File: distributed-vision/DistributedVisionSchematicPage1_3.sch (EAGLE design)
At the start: 131 parts, among them J1 RASPBERRRY_COMPUTE_CM3, J2 RASPBERRRY_COMPUTE_CM3, J3 XS10, J6 DM3D-SF, J7 10029449-111RLF, J8 1-84952-5, J9 1-84952-5, Q1 AP2331SA-7, Q2 BSS127, Q3 BSS127, Q4 BSS127, Q5 PSMN014-40YS, U1 TPS70625DBVR, U2 LM26420XMH, U4 ESD224, X1 JST-XH-02-PIN-LONG-PAD

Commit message: Combined all Schematic Pages
Fixed some Capacitor/Resistor Values
Began integrating POE
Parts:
- added C14, C64: 1u, rcl:C-USC0402
- added C53, C54, C59, C60, C63, C68: 100n, rcl:C-USC0402
- added C55, C61, C67: 10n, rcl:C-USC0402
- added C56: 1nF, rcl:C-USC0402
- added C57, C73: 10u, rcl:C-USC0402
- added C62: 4u7, rcl:C-USC0402
- added C65, C66: 33p, rcl:C-USC0402
- added C74: 22n, rcl:C-USC0402
- added IC1: IPB180N06S4-H1, infineon:IPB180N06S4-H1
- added J10: USBR-A-D-F-O-TH, distributed-vision:USBR-A-D-F-O-TH
- added J11: (no value), con-amp:215875-3
- added J12: ARJM11C7-104-AB-EW2, ethernet_poe_v2.1:ARJM11C7-104-AB-EW2
- added J4: RASPBERRRY_COMPUTE_CM3, distributed-vision:RASPBERRRY_COMPUTE_CM3
- added J5: 1981584-1, RoboJackets-Connectors:1981584-1
- added L3, L6: 2A 120r, RoboJackets-Inductors:INDUCTOR_0805
- added L4, L7: 1.3A 120r, RoboJackets-Inductors:INDUCTOR_0805
- added LED1, LED2, LED3: LAP4-BOTTOM, led:LAP4-BOTTOM
- added Q6: 25 MHz, crystal:FA-20H
- added R18: 47k, RoboJackets-Resistors:ERJ-L06KF50MV
- added R19, R28, R31, R40, R51: 4k7, RoboJackets-Resistors:ERJ-L06KF50MV
- added R26: 12k, RoboJackets-Resistors:ERJ-L06KF50MV
- added R27: 12k4, RoboJackets-Resistors:ERJ-L06KF50MV
- added R29, R30, R32: 470r, RoboJackets-Resistors:ERJ-L06KF50MV
- added R33, R34, R35, R36: 49r9, RoboJackets-Resistors:ERJ-L06KF50MV
- added R37: 10r, RoboJackets-Resistors:ERJ-L06KF50MV
- added R39, R41: 1M, RoboJackets-Resistors:ERJ-L06KF50MV
- added T1, T2: (no value), transistor:MUN2211T1-NPN_DRIVER-SC59-BEC
- added U3: LAN9513-JZXQFN64_9X9MC_MCH-M, distributed-vision:LAN9513-JZXQFN64_9X9MC_MCH-M
- added U5: FSUSB42MUX, distributed-vision:FSUSB42MUX
- added U6, U7, U8, U9: SP3003-02, distributed-vision:SP3003-02
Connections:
- new net N$55: C64.1, L4.1, U3.VDD18USBPLL
- new net N$56: C63.1, L4.2, U3.VDD18ETHPLL
- new net N$57: R29.PIN2, U3.NFDX_LED/GPIO0
- new net N$58: R30.PIN2, U3.NLNKA_LED/GPIO1
- new net N$59: R32.PIN2, U3.NSPD_LED/GPIO2
- new net N$60: LED3.C, R29.PIN1
- new net N$61: C53.1, R31.PIN1, T1.C, T2.C, U3.NRESET
- new net N$62: T1.B, T2.B
- new net N$63: R40.PIN1, U3.NTRST, U3.TCK, U3.TDI, U3.TMS
- new net N$64: Q6.2, U3.XI
- new net N$65: Q6.4, U3.XO
- new net N$66: C66.1, Q6.1, R39.PIN2
- new net N$67: C65.1, Q6.3, R39.PIN1
- new net N$68: IC1.D, R18.PIN1, U5.SEL
- new net N$69: R26.PIN1, U3.USBRBIAS
- new net N$70: R28.PIN1, U3.AUTOMDIX_EN
- new net N$71: R27.PIN1, U3.EXRES
- new net N$72: J5.1, L3.2, U6.VCC
- new net N$73: C57.1, C59.1, C67.1, J11.1, L6.2, U7.VCC
- new net N$74: C74.1, J12.CT, R37.PIN1
- new net N$75: C54.1, C55.1, R18.PIN2
- new net VCC: IC1.G, J12.G_LED+, J12.Y_LED+, L3.1, L6.1, L7.1, LED1.A, LED2.A, LED3.A, R19.PIN1, R28.PIN2, R31.PIN2, R33.PIN2, R34.PIN2, R35.PIN2, R36.PIN2, R37.PIN2, R40.PIN2, U3.TEST3, U3.VBUS_DET, U3.VDD33A, U3.VDD33IO, U5.VCC
- net FB1: now also J2D.NC@1, J2D.NC@2; no longer J2D.SDX_VDD, J2D.SDX_VDD1
- net GND: now also C14.2, C53.2, C54.2, C55.2, C56.1, C56.2, C57.2, C59.2, C60.2, C61.2, C62.2, C63.2, C64.2, C65.2, C66.2, C67.2, C68.2, C73.2, C74.2, IC1.S, J10.BGND, J10.TGND, J11.4, J12.CHASSIS1, J12.CHASSIS2, J5.5, J5.SHIELD, R19.PIN2, R26.PIN2, R27.PIN2, R41.PIN1, R41.PIN2, R51.PIN2, T1.E, T2.E, U3.CLK24_EN, U3.TEST2, U5.!OE, U5.GND, U7.GND, U8.GND, U9.GND
- net N$1: now also C14.1, C60.1, C61.1, C62.1, U3.VDD18CORE
- net N$17: now also J4A.USB_DP, U5.D+
- net N$18: now also J4A.USB_DM, U5.D-
- net N$19: now also J4A.USB_OTGID, R51.PIN1
- net N$22: now also U3.USBDP0, U5.HSD2+
- net N$23: now also U3.USBDM0, U5.HSD2-
- net N$26: now also J5.3, U5.HSD1+, U6.IO1
- net N$27: now also J5.2, U5.HSD1-, U6.IO2
- net N$29: now also J10.BD-, U3.USBDM2, U9.IO1
- net N$30: now also J10.BD+, U3.USBDP2, U9.IO2
- net N$31: now also J10.TD-, U3.USBDM3, U8.IO1, U8.IO2
- net N$32: now also J10.TD+, U3.USBDP3
- net N$34: now also J12.TD+, R33.PIN1, U3.TXP
- net N$35: now also J12.TD-, R34.PIN1, U3.TXN
- net N$36: now also J11.2, U3.USBDM4, U7.IO1, U7.IO2
- net N$37: now also J11.3, U3.USBDP4
- net N$38: now also J12.RD+, R35.PIN1, U3.RXP
- net N$39: now also J12.RD-, R36.PIN1, U3.RXN
- net N$41: now also J10.BVCC
- net N$42: now also C68.1, C73.1, J10.TVCC, L7.2, U8.VCC, U9.VCC
- net N$8: now also J12.G_LED-, LED2.C, R30.PIN1
- net N$9: now also J12.Y_LED-, LED1.C, R32.PIN1
- net SD_CLK: now also J2D.NC@3; no longer J2D.SDX_CLK
- net SD_CMD: now also J2D.NC@4; no longer J2D.SDX_CMD
- net SD_DAT0: now also J2D.NC@5; no longer J2D.SDX_D0
- net SD_DAT1: now also J2D.NC@6; no longer J2D.SDX_D1
- net SD_DAT2: now also J2D.NC@7; no longer J2D.SDX_D2
- net SD_DAT3: now also J2D.NC@8; no longer J2D.SDX_D3

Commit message: Cleaning up Schematic
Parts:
- removed C1, C2, C30, C31, C32: (no value), rcl:C-USC0603
- removed DQ1, DQ2, DQ6: GREEN, RoboJackets-LEDs:LED-GREEN0603
- removed J4: RASPBERRRY_COMPUTE_CM3, distributed-vision:RASPBERRRY_COMPUTE_CM3
- removed R15, R17, R2, R3, R45, R5, R6: (no value), rcl:R-US_R0603
- removed T2: (no value), transistor:MUN2211T1-NPN_DRIVER-SC59-BEC
- removed U1: TPS70625DBVR, distributed-vision:TPS70625DBVR
- removed VD4: 60V, RoboJackets-Diodes:DFLS160-7
- added C75, C86: (no value), rcl:C-USC0603
- added D1, D2, D6: GREEN, RoboJackets-LEDs:LED-GREEN0603
- added D4: 60V, RoboJackets-Diodes:DFLS160-7
- added R38, R42, R43, R46, R47, R48: (no value), rcl:R-US_R0603
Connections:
- net N$10 renamed GPIO17
- net N$11 renamed GPIO26
- net N$12 renamed CAM1_CP
- net N$13 renamed CAM1_CN
- net N$14 renamed CAM1_DP1
- net N$15 renamed CAM1_DN1
- net N$16 renamed CAM1_DP0
- net N$20 renamed CAM0_DN1
- net N$21 renamed CAM0_DP1
- net N$24 renamed HDMI_D2_P
- net N$25 renamed HDMI_D2_N
- net N$28 renamed HDMI_D0_P
- net N$3 renamed GPIO11
- net N$43 renamed HDMI_CLK_N
- net N$44 renamed 5V/R53
- net N$6 renamed GPIO10
- net N$7 renamed GPIO09
- removed net N$2: C1.1, J1B.GPIO0-27_VDD@1, J1B.GPIO0-27_VDD@2, R2.2, R3.2
- removed net N$29: J10.BD-, J2A.HDMI_D0_N, J7.9, U3.USBDM2, U9.IO1
- removed net N$4: C2.1, J1B.GPIO28-45_VDD@1, J1B.GPIO28-45_VDD@2, R5.2, R6.2
- removed net N$54: J2A.HDMI_SCL, J7.15, R54.1, U4.IO3_C
- removed net N$62: T1.B, T2.B
- new net 3V3: C3.1, J3.3V3@1, J3.3V3@2
- new net 5V/R54: J7.15
- new net CAM0_CN: J2A.CAM0_CN, J9.8
- new net CAM0_CP: J2A.CAM0_CP, J9.9
- new net CAM0_DN0: J2A.CAM0_DN0, J9.2
- new net CAM0_DP0: J2A.CAM0_DP0, J9.3
- new net CAM1_DN0: J2A.CAM1_DN0, J8.2
- new net GPIO22: J2A.GPIO22
- new net GPIO27: J2A.GPIO27, J3.GPIO27
- new net HDMI_CLK_P: J2A.HDMI_CLK_P, J7.10
- new net HDMI_D0_N: J2A.HDMI_D0_N, J7.9
- new net HDMI_D1_N: J2A.HDMI_D1_N, J7.6
- new net HDMI_D1_P: J2A.HDMI_D1_P, J7.4
- new net HDMI_SCL: J2A.HDMI_SCL, R54.1, U4.IO3_C
- new net N$12: C75.1, J2B.GPIO0-27_VDD@1, J2B.GPIO0-27_VDD@2, R38.2, R42.2
- new net N$17/1.6C: J2A.USB_DP
- new net N$18/1.6B: J2A.USB_DM
- new net N$24: C86.1, J2B.GPIO28-45_VDD@1, J2B.GPIO28-45_VDD@2, R43.2, R46.2
- new net NS$19/1.6B: J2A.USB_OTGID
- new net USBDM2: J10.BD-, U3.USBDM2, U9.IO1
- new net USBDP2: U3.USBDP2
- net +1.8V: now also J2B.1V8@1, J2B.1V8@2, J2B.1V8@3, J2B.1V8@4, R38.1, R43.1; no longer J1B.1V8@1, J1B.1V8@2, J1B.1V8@3, J1B.1V8@4, R3.1, R6.1
- net +2.5V: no longer C31.1, C32.1, R45.2, U1.OUT
- net +5V: now also D2.A, D4.A, D4.C, R47.1; no longer DQ2.A, R15.1, VD4.A, VD4.C
- net EMMC_DISABLE_N: now also J2A.!EMMC_DISABLE; no longer J1A.!EMMC_DISABLE
- net EMMC_EN_N_1V8: now also J2B.EMMC_EN_N_1V8; no longer J1B.EMMC_EN_N_1V8
- net FB1: now also D1.A, D6.A, J2B.3V3@1, J2B.3V3@2, J2B.3V3@3, J2B.3V3@4, J2D.SDX_VDD, J2D.SDX_VDD1, R42.1, R46.1, R48.1; no longer C3.1, C30.1, DQ1.A, DQ6.A, J1B.3V3@1, J1B.3V3@2, J1B.3V3@3, J1B.3V3@4, J2D.NC@1, J2D.NC@2, J3.3V3@1, J3.3V3@2, R17.1, R2.1, R45.1, R5.1, U1.EN, U1.IN
- net GND: now also C75.2, C86.2, J3.GND@7, U6.GND; no longer C1.2, C2.2, C30.2, C31.2, C32.2, T2.E, U1.GND
- net N$17: no longer J2A.CAM1_DN0, J4A.USB_DP, J8.2
- net N$18: no longer J2A.CAM0_DN0, J4A.USB_DM, J9.2
- net N$19: no longer J2A.CAM0_DP0, J4A.USB_OTGID, J9.3
- net N$22: no longer J2A.CAM0_CN, J9.8
- net N$23: no longer J2A.CAM0_CP, J9.9
- net N$26: no longer J2A.HDMI_D1_P, J7.4
- net N$27: no longer J2A.HDMI_D1_N, J7.6
- net N$30: no longer U3.USBDP2
- net N$32: now also D6.C; no longer DQ6.C
- net N$34: now also D1.C; no longer DQ1.C
- net N$35: now also D2.C; no longer DQ2.C
- net N$42: no longer J2A.HDMI_CLK_P, J7.10
- net N$61: no longer T2.C
- net N$8: no longer J2A.GPIO22, J3.GPIO22
- net N$9: no longer J2A.GPIO27, J3.GPIO27
- net SD_CLK: now also J2D.SDX_CLK; no longer J2D.NC@3
- net SD_CMD: now also J2D.SDX_CMD; no longer J2D.NC@4
- net SD_DAT0: now also J2D.SDX_D0; no longer J2D.NC@5
- net SD_DAT1: now also J2D.SDX_D1; no longer J2D.NC@6
- net SD_DAT2: now also J2D.SDX_D2; no longer J2D.NC@7
- net SD_DAT3: now also J2D.SDX_D3; no longer J2D.NC@8
- net VBATT: now also J2B.VBAT@1, J2B.VBAT@2, J2B.VBAT@3, J2B.VBAT@4, R47.2, R48.2; no longer J1B.VBAT@1, J1B.VBAT@2, J1B.VBAT@3, J1B.VBAT@4, R15.2, R17.2
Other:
- note removed: "DAC VCC"
- moved on the sheet: C10, C102, C103, C12, C13, C15, C16, C17, C18, C19, C20, C21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

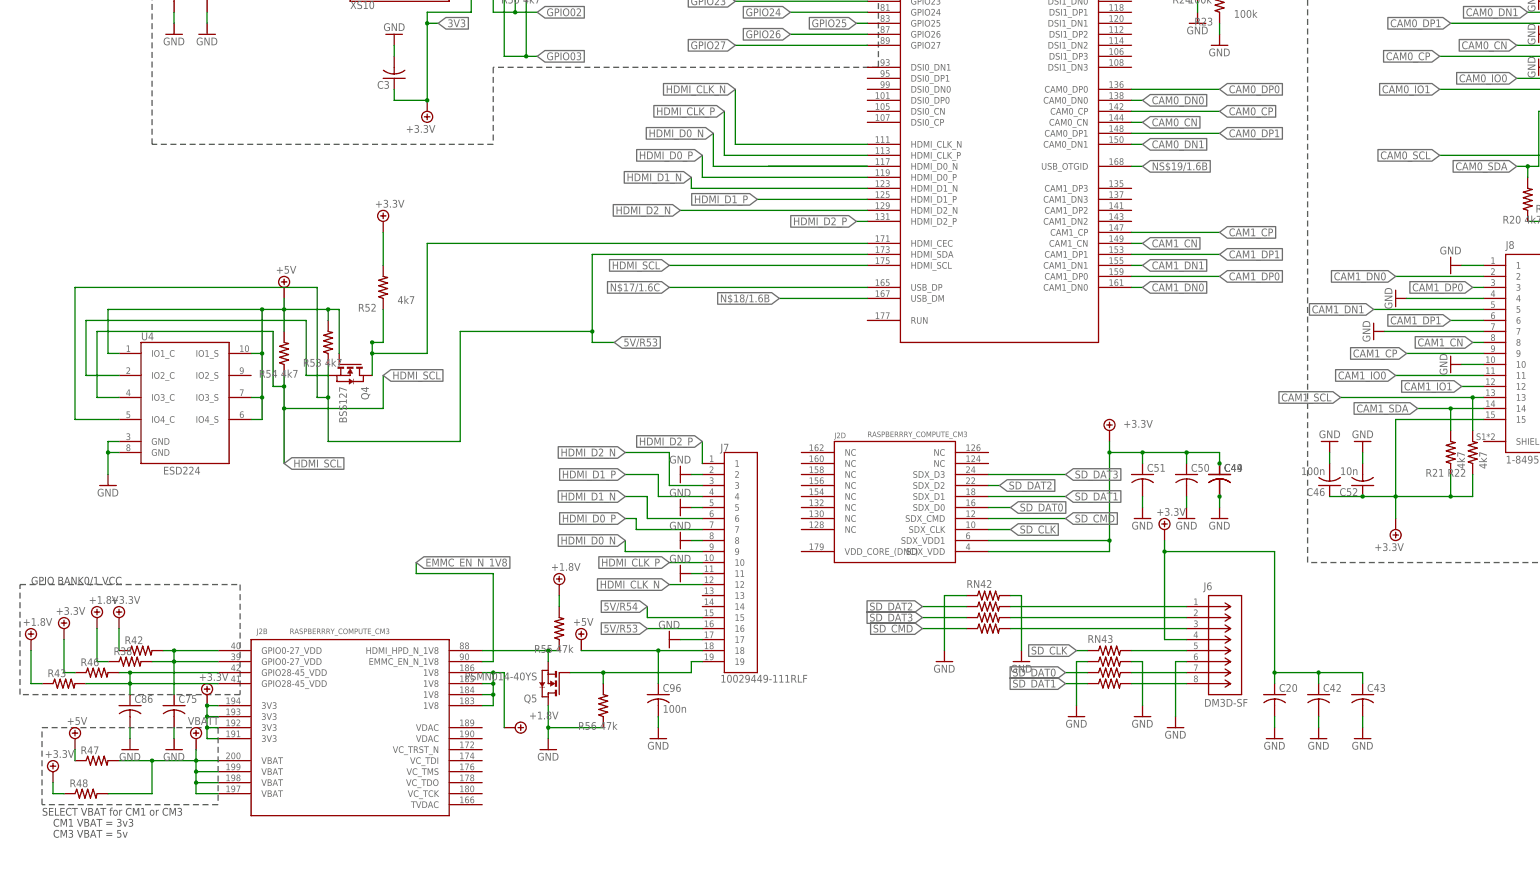
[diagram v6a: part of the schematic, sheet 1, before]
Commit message: Cleaned up Schematic
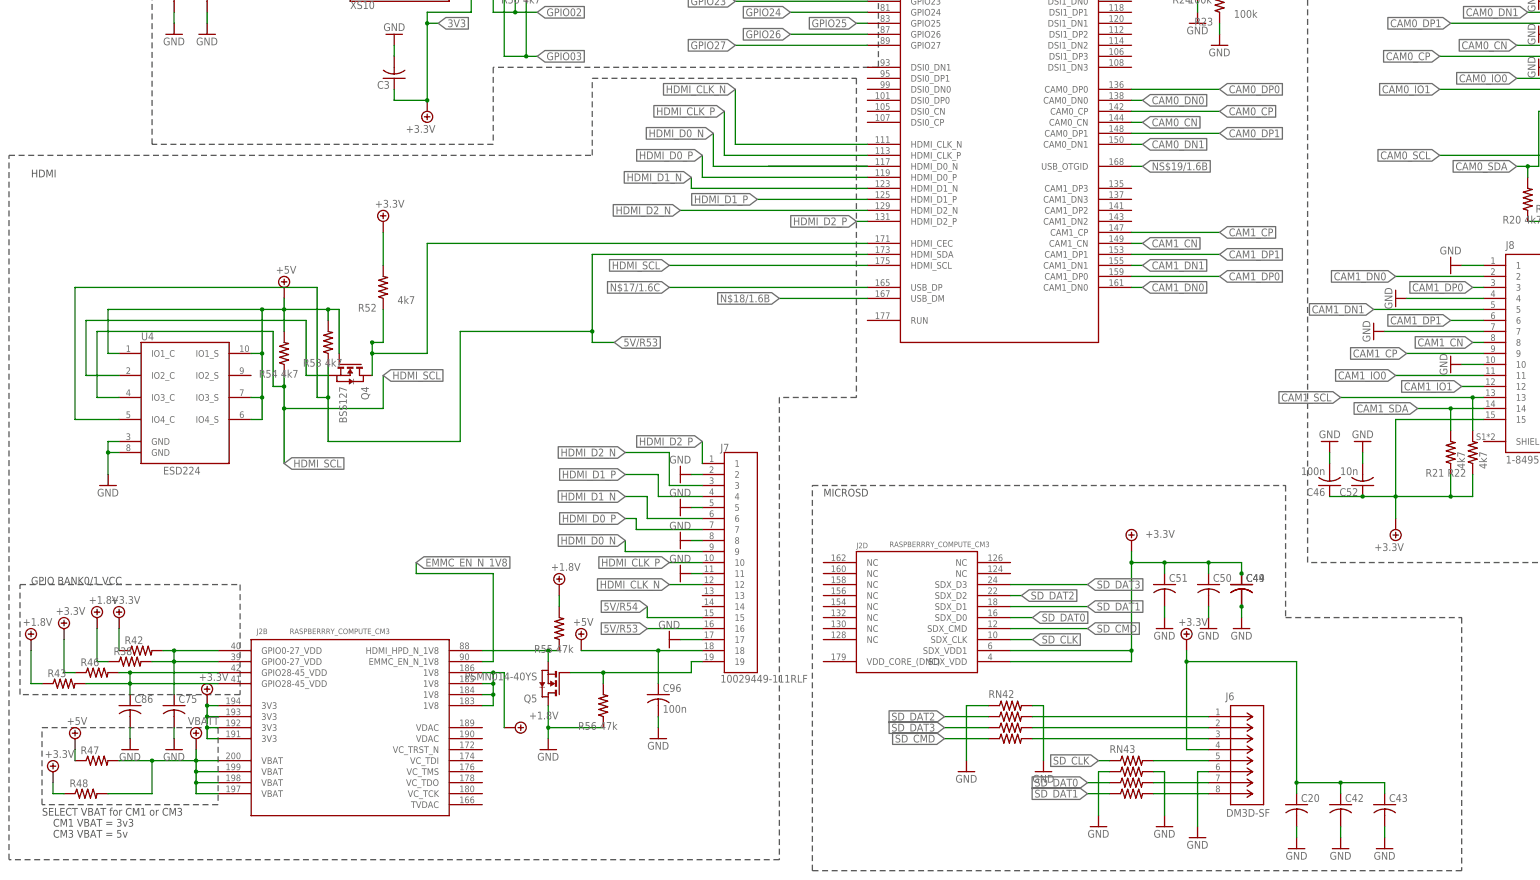
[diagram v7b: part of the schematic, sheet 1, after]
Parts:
- removed J11: (no value), con-amp:215875-3
- added JP2: (no value), RoboJackets-Connectors:PINHD-1X4
- C10, C15, C16, C21, C36, C39, C40, C48, C5, C6, C69, C70, C71, C72, C78, C79, C81, C82, C84, C88, C91: value (none) -> 100n
- C102, C103, C12, C17, C22, C35, C47, C7: value (none) -> 10u
- C13, C18, C19, C33, C38, C4, C41, C76, C77, C8, C80, C85, C9: value (none) -> 10n
- C37: value (none) -> 22u
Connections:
- net GND: now also JP2.4; no longer J11.4
- net N$36: now also JP2.2; no longer J11.2
- net N$37: now also JP2.3; no longer J11.3
- net N$73: now also JP2.1; no longer J11.1
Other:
- note added: "HDMI"
- note added: "MICROSD"
- moved on the sheet: C20, C42, C43, C44, C49, C50, C51, J10, J2D, J6, RN42, RN43

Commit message: Integrated PoE
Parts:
- removed C74: 22n, rcl:C-USC0402
- removed R33, R34, R35, R36: 49r9, RoboJackets-Resistors:ERJ-L06KF50MV
- removed R37: 10r, RoboJackets-Resistors:ERJ-L06KF50MV
- added C117, C121: 10000pF, rcl:C-USC0603
- added C118, C119, C139: 10000pF, adafruit:C-USC0402
- added C120, C133, C134, C135, C136, C137, C138, C142, C148: 0.1uF, adafruit:C-USC0402
- added C122: 10000pF, 50V, rcl:C-USC0603
- added C123: 0.022uF, 50V, rcl:C-USC0603
- added C124, C126: 0.220uF, rcl:C-USC0603
- added C125: 100uF, rcl:CPOL-USE2-5
- added C127: 1uF, 50V, rcl:C-USC0603
- added C128: 2.2uF, 50V, rcl:C-USC0603
- added C129: 100uF, 35V, rcl:CPOL-USE2.5-7
- added C130, C131: 18pF, rcl:C-USC0603
- added C132: 22uF, SparkFun-Capacitors:22UF-POLAR-PANASONIC_C-35V-20%
- added C140: 4.7uF, rcl:C-USC0603
- added C141: 22uF, rcl:C-USC0603
- added C144, C145: 0.1uF, adafruit:C-USC0603
- added C146, C147: 1uF, rcl:C-USC0603
- added D10, D11: NTS260ESFT3G, ethernet_poe:NTS260ESFT3G
- added D3, D5, D7: GRN, led:LEDCHIP-LED0603
- added D8: YLW, led:LEDCHIP-LED0603
- added D9: BLU, led:LEDCHIP-LED0603
- added F2: 1A (Trip), ethernet_poe:0ZCG0050AF2C
- added FB1: 742792023, ethernet_poe:742792023
- added H1, H2: MOUNT-PAD-ROUND2.8, holes:MOUNT-PAD-ROUND2.8
- added J11: (no value), SparkFun-Connectors:CONN_07
- added J4: (no value), SparkFun-Connectors:CONN_05
- added L5: MPZ2012S601AT000, POE:MPZ2012S601AT000
- added L9: 47uH, ethernet_poe_v2.1:7447709470_7447709470
- added R100, R74, R75, R98, R99: 470, rcl:R-US_R0603
- added R73, R76: 75, 1%, rcl:R-US_R0603
- added R77: 22, 1%, rcl:R-US_R0603
- added R78, R79, R88, R89, R90, R91, R92, R95: 10k, rcl:R-US_R0603
- added R80, R81: 49.9, 1%, adafruit:R-US_R0402
- added R82: 22k, rcl:R-US_R0603
- added R83: 715k, 1%, rcl:R-US_R0603
- added R84: 20k, 1%, rcl:R-US_R0603
- added R85: 30.1k, 1%, rcl:R-US_R0603
- added R86: 11.8k, 1%, rcl:R-US_R0603
- added R87: 66.5k, 1%, rcl:R-US_R0603
- added R93: 1M, adafruit:R-US_R0402
- added R94: 12.4k, 1%, rcl:R-US_R0603
- added R96: 4.7k, rcl:R-US_R0603
- added R97: 330, rcl:R-US_R0603
- added S1: KMR2, RoboJackets-Switches:KMR2
- added U1: W5500, ethernet_poe:W5500
- added U10: AZ1117EH-3.3TRG1, ethernet_poe:AZ1117EH-3.3TRG1
- added U11: IFX91041, ethernet_poe:IFX91041
- added U12: TPS26600PWPR, ethernet_poe:TPS26600PWPR
- added X2: 25MHz, ethernet_poe_v2.1:ABM10W-25.0000MHZ-6-K1Z-T3
- J12: device ethernet_poe_v2.1:ARJM11C7-104-AB-EW2 -> ethernet_poe:ARJM11C7-104-AB-EW2
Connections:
- removed net N$35: D2.C, J12.TD-, R25.2, R34.PIN1, U3.TXN
- removed net N$38: J12.RD+, R35.PIN1, R9.2, U2.PGND_2, U3.RXP
- removed net N$39: J12.RD-, L1.1, R36.PIN1, U2.SW1, U3.RXN
- removed net N$74: C74.1, J12.CT, R37.PIN1
- new net !INT: J11.1, R89.2, U1.!INTN
- new net !RST: C148.1, J4.2, R95.1, S1.2, U1.!RSTN
- new net !SCS: J11.5, R88.2, U1.!SCSN
- new net +24V: C127.1, J12.VC1+, R83.1, U12.!SHDN, U12.IN
- new net +24V_FUSE: C122.1, C129.+, J4.1, R96.1, U11.EN, U11.VS, U12.OUT
- new net +3V3_A: C132.+, C133.1, C134.1, C135.1, C136.1, C137.1, C138.1, C144.1, FB1.1, R77.2, R80.1, R81.2, U1.AVDD
- new net +3V3_D: C141.1, C142.1, C145.1, C147.1, D11.2, FB1.2, J4.4, R100.1, R74.1, R75.1, R88.1, R89.1, R90.2, R91.2, R92.2, R95.2, R98.1, R99.1, U1.VDD, U10.OUT
- new net +5V_PREFUSE: C125.+, C126.1, F2.1, L9.2, U11.FB
- new net 24V_LED: D3.A, R96.2
- new net 24_LOAD: J11.7, R87.1, U12.IMON
- new net 3V3_LED: D7.A, R98.2
- new net 3V3_LED1: D8.A, R99.2
- new net 3V3_LED2: D9.A, R100.2
- new net 5V_LED: D5.A, R97.2
- new net 5V_RAW: C124.2, D10.1, L9.1, U11.BUO
- new net ACTLED: D8.C, U1.ACTLED
- new net AGND: H1.MOUNT, H2.MOUNT, J12.CHASSIS1, J12.CHASSIS2, L5.2
- new net CT: C120.1, J12.CT, R77.1
- new net DUPLED: D9.C, U1.DUPLED
- new net G_LED+: J12.G_LED+, R75.2
- new net MISO: J11.3, U1.MISO
- new net MOSI: J11.2, U1.MOSI
- new net N$10: J12.VC2+, R73.2
- new net N$11: C131.1, R93.1, U1.XO, X2.OUT
- new net N$13: C130.1, R93.2, U1.XI, X2.IN
- new net N$14: J12.VC2-, R76.2
- new net N$15: C124.1, U11.BDS
- new net N$16: C123.2, R82.1
- new net N$2: C139.1, U1.1V2O
- new net N$20: C117.2, R73.1, R76.1
- new net N$21: R94.2, U1.EXRES1
- new net N$25: R83.2, R84.1, U12.UVLO
- new net N$28: R84.2, R85.1, U12.OVP
- new net N$29: C128.1, U12.DVDT
- new net N$3: C140.1, U1.TOCAP
- new net N$4: C123.1, U11.COMP
- new net N$7: R90.1, U1.PMODE0
- new net NLINKA_LED: J12.G_LED-, LED2.C, R30.PIN1, U1.LINKLED
- new net NSPD_LED: J12.Y_LED-, LED1.C, R32.PIN1, U1.SPDLED
- new net RD_N: C119.2, J12.RD-
- new net RD_P: C118.2, J12.RD+
- new net RTN: C128.2, R85.2, R86.2, R87.2, U12.MODE, U12.PAD, U12.RTN
- new net RX_FILTER: C121.1, R78.2, R79.2
- new net RX_N: C119.1, L1.1, R79.1, U1.RXN, U2.SW1, U3.RXN
- new net RX_P: C118.1, R78.1, R9.2, U1.RXP, U2.PGND_2, U3.RXP
- new net SCLK: J11.4, U1.SCLK
- new net TX_N: D2.C, J12.TD-, R25.2, R80.2, U1.TXN, U3.TXN
- new net TX_P: D1.C, J12.TD+, R12.2, R81.1, U1.TXP, U3.TXP
- new net Y_LED+: J12.Y_LED+, R74.2
- net +5V: now also C146.1, D11.1, F2.2, J4.3, R97.1, U10.IN
- net GND: now also C117.1, C120.2, C121.2, C122.2, C125.-, C126.2, C127.2, C129.-, C130.2, C131.2, C132.-, C133.2, C134.2, C135.2, C136.2, C137.2, C138.2, C139.2, C140.2, C141.2, C142.2, C144.2, C145.2, C146.2, C147.2, C148.2, D10.2, D3.C, D5.C, D7.C, J11.6, J12.VC1-, J4.5, L5.1, R82.2, R94.1, S1.1, U1.AGND, U1.GND, U10.ADJ/GND, U11.GND, U11.SYNC, U12.GND, X2.SHD1, X2.SHD2; no longer C74.2, J12.CHASSIS1, J12.CHASSIS2
- net N$34: now also R86.1, U12.ILIM; no longer D1.C, J12.TD+, R12.2, R33.PIN1, U3.TXP
- net N$8: now also R91.1, U1.PMODE1; no longer J12.G_LED-, LED2.C, R30.PIN1
- net N$9: now also R92.1, U1.PMODE2; no longer J12.Y_LED-, LED1.C, R32.PIN1
- net VCC: no longer J12.G_LED+, J12.Y_LED+, R33.PIN2, R34.PIN2, R35.PIN2, R36.PIN2, R37.PIN2
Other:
- note added: "!FLT left floating"
- note added: "#3 (or M2.5) Drill Size"
- note added: "1.8A Rated"
- note added: "1A Rated"
- note added: "24V to 5V"
- note added: "3.3V Analog"
- note added: "5V to 3.3V"
- note added: "B Mode Configuration with 24V passive"
- note added: "Chassis Ground"
- note added: "Control"
- note added: "Ethernet"
- note added: "Filtering"
- note added: "Fuse"
- note added: "Headers"
- note added: "LEDs"
- note added: "L_out = ((V_in - V_out) * V_out)/ (I_rip * f_s * V_in) 42.7uF = ((24-5)*5)/(0.25*370000*24) I_sat > 3.5A"
- note added: "Mounting Holes"
- note added: "NOTE: This pi filter isolates the digital and analog 3.3V power supplies by attenuating differential mode noise."
- note added: "Power (24V-5V)"
- note added: "Power (5V-3.3V)"
- note added: "R(ILIM) = 12 / ILIM ILIM = 1 A"
- note added: "R30, R31, R32 Configure OverV, UnderV"
- note added: "R34 = V(IMONmax)/(I(ILIM)*75*10^-6) V(IMONmax) = max ADC voltage = 5V"
- note added: "RC to debounce switch"
- note added: "Reset"
- note added: "Undervoltage = 18V Overvoltage = 30V Current Limit = 1A"
- note added: "V(ovpr)= R32/(R30+R31+R32) * V(ov)"
- note added: "V(uvpr)= R31+R32/(R30+R31+R32) *V(uv)"
